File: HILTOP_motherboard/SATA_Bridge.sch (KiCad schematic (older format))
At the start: 60 parts, among them J25 DEBUG, U37 TUSB9261, U38 AT25DN512CSSHF-B, Y7 40MHz Crystal

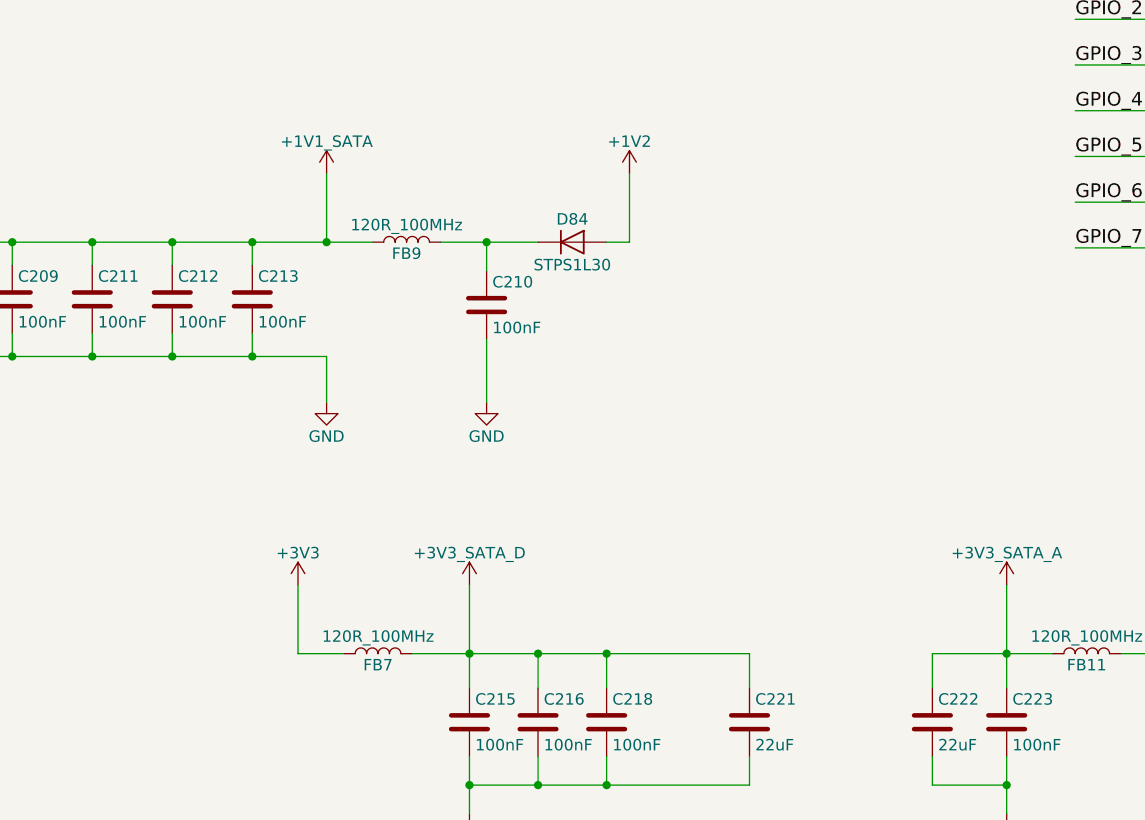
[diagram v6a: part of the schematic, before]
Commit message: DRC checks complete, all errors and warnings cleared. BOM created and parts rationalised.
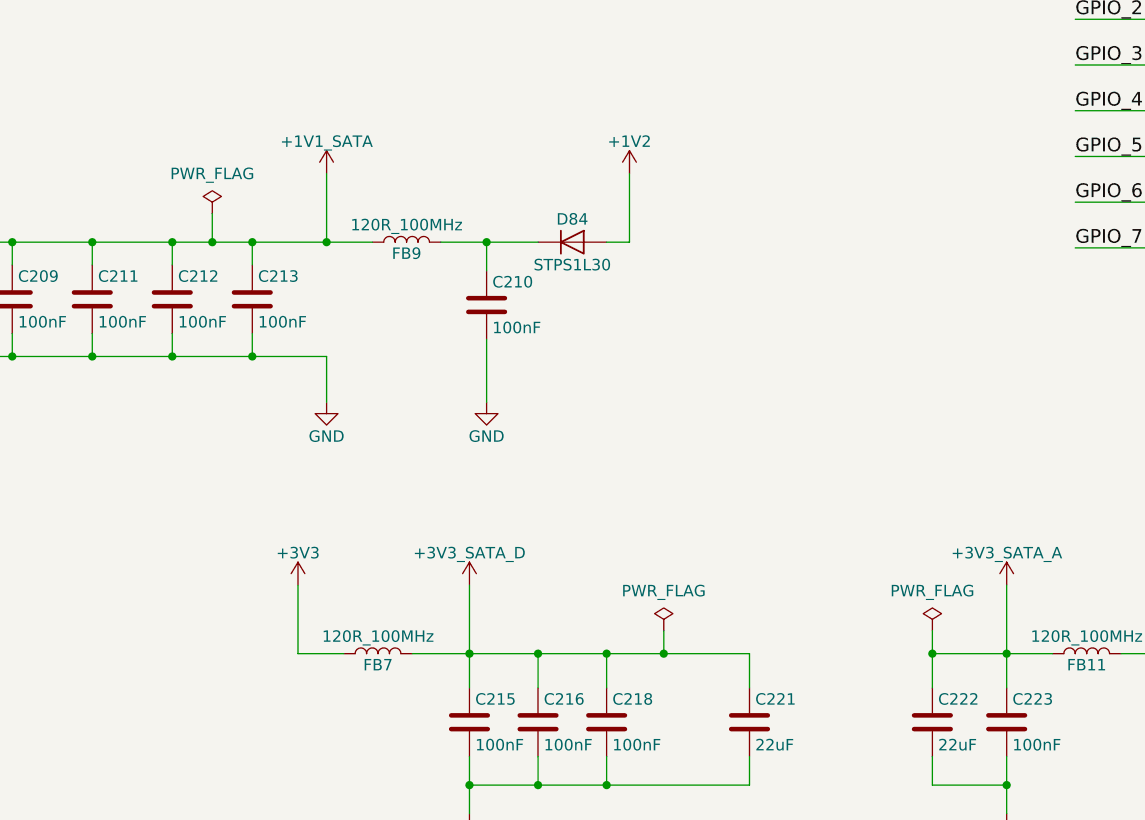
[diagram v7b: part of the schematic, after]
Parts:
- C195: Devtank 105-012 -> 105-014
- C196, C221, C222: footprint Capacitor_SMD:C_0805_2012Metric -> Capacitor_SMD:C_1206_3216Metric; Devtank 105-018 -> 105-003
- R235, R236, R237, R238, R239, R240, R241, R242: Devtank 101-024 -> 101-504
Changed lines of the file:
@@
 F 0 "C221" H 8050 10200 50  0000 L CNN
 F 1 "22uF" H 8050 10000 50  0000 L CNN
-F 2 "Capacitor_SMD:C_0805_2012Metric" H 8063 9950 50  0001 C CNN
+F 2 "Capacitor_SMD:C_1206_3216Metric" H 8063 9950 50  0001 C CNN
 F 3 "" H 8025 10100 50  0000 C CNN
-F 4 "105-018" H 8025 10100 50  0001 C CNN "Devtank"
+F 4 "105-003" H 8025 10100 50  0001 C CNN "Devtank"
 	1    8025 10100
 	1    0    0    -1
@@
 F 0 "C222" H 8850 10200 50  0000 L CNN
 F 1 "22uF" H 8850 10000 50  0000 L CNN
-F 2 "Capacitor_SMD:C_0805_2012Metric" H 8863 9950 50  0001 C CNN
+F 2 "Capacitor_SMD:C_1206_3216Metric" H 8863 9950 50  0001 C CNN
 F 3 "" H 8825 10100 50  0000 C CNN
-F 4 "105-018" H 8825 10100 50  0001 C CNN "Devtank"
+F 4 "105-003" H 8825 10100 50  0001 C CNN "Devtank"
 	1    8825 10100
 	1    0    0    -1
@@
 F 0 "C196" H 2675 8350 50  0000 L CNN
 F 1 "22uF" H 2675 8150 50  0000 L CNN
-F 2 "Capacitor_SMD:C_0805_2012Metric" H 2688 8100 50  0001 C CNN
+F 2 "Capacitor_SMD:C_1206_3216Metric" H 2688 8100 50  0001 C CNN
 F 3 "" H 2650 8250 50  0000 C CNN
-F 4 "105-018" H 2650 8250 50  0001 C CNN "Devtank"
+F 4 "105-003" H 2650 8250 50  0001 C CNN "Devtank"
 	1    2650 8250
 	1    0    0    -1
@@
 F 2 "Capacitor_SMD:C_0603_1608Metric" H 2338 8100 50  0001 C CNN
 F 3 "" H 2300 8250 50  0000 C CNN
-F 4 "105-012" H 2300 8250 50  0001 C CNN "Devtank"
+F 4 "105-014" H 2300 8250 50  0001 C CNN "Devtank"
 	1    2300 8250
 	1    0    0    -1
@@
 F 2 "Resistor_SMD:R_0402_1005Metric" V 11355 6625 50  0001 C CNN
 F 3 "" H 11425 6625 50  0000 C CNN
-F 4 "101-024" V 11425 6625 60  0001 C CNN "Devtank"
+F 4 "101-504" V 11425 6625 60  0001 C CNN "Devtank"
 	1    11425 6625
 	0    1    1    0
@@
 F 2 "Resistor_SMD:R_0402_1005Metric" V 11355 6825 50  0001 C CNN
 F 3 "" H 11425 6825 50  0000 C CNN
-F 4 "101-024" V 11425 6825 60  0001 C CNN "Devtank"
+F 4 "101-504" V 11425 6825 60  0001 C CNN "Devtank"
 	1    11425 6825
 	0    1    1    0
@@
 F 2 "Resistor_SMD:R_0402_1005Metric" V 11355 7025 50  0001 C CNN
 F 3 "" H 11425 7025 50  0000 C CNN
-F 4 "101-024" V 11425 7025 60  0001 C CNN "Devtank"
+F 4 "101-504" V 11425 7025 60  0001 C CNN "Devtank"
 	1    11425 7025
 	0    1    1    0
@@
 F 2 "Resistor_SMD:R_0402_1005Metric" V 11355 7225 50  0001 C CNN
 F 3 "" H 11425 7225 50  0000 C CNN
-F 4 "101-024" V 11425 7225 60  0001 C CNN "Devtank"
+F 4 "101-504" V 11425 7225 60  0001 C CNN "Devtank"
 	1    11425 7225
 	0    1    1    0
@@
 F 2 "Resistor_SMD:R_0402_1005Metric" V 11355 7425 50  0001 C CNN
 F 3 "" H 11425 7425 50  0000 C CNN
-F 4 "101-024" V 11425 7425 60  0001 C CNN "Devtank"
+F 4 "101-504" V 11425 7425 60  0001 C CNN "Devtank"
 	1    11425 7425
 	0    1    1    0
@@
 F 2 "Resistor_SMD:R_0402_1005Metric" V 11355 7625 50  0001 C CNN
 F 3 "" H 11425 7625 50  0000 C CNN
-F 4 "101-024" V 11425 7625 60  0001 C CNN "Devtank"
+F 4 "101-504" V 11425 7625 60  0001 C CNN "Devtank"
 	1    11425 7625
 	0    1    1    0
@@
 F 2 "Resistor_SMD:R_0402_1005Metric" V 11355 7825 50  0001 C CNN
 F 3 "" H 11425 7825 50  0000 C CNN
-F 4 "101-024" V 11425 7825 60  0001 C CNN "Devtank"
+F 4 "101-504" V 11425 7825 60  0001 C CNN "Devtank"
 	1    11425 7825
 	0    1    1    0
@@
 F 2 "Resistor_SMD:R_0402_1005Metric" V 11355 8025 50  0001 C CNN
 F 3 "" H 11425 8025 50  0000 C CNN
-F 4 "101-024" V 11425 8025 60  0001 C CNN "Devtank"
+F 4 "101-504" V 11425 8025 60  0001 C CNN "Devtank"
 	1    11425 8025
 	0    1    1    0
@@
 	5150 8000 5500 8000
 Wire Wire Line
-	5500 8000 5850 8000
+	5500 8000 5675 8000
 Wire Wire Line
 	5500 8500 5850 8500
@@
 	3000 8000 3750 8000
 Wire Wire Line
-	7400 9800 8025 9800
+	7400 9800 7650 9800
 Wire Wire Line
 	7400 10375 8025 10375
+$Comp
+L power:PWR_FLAG #FLG0131
+U 1 1 5EB53667
+P 7650 9700
+F 0 "#FLG0131" H 7650 9775 50  0001 C CNN
+F 1 "PWR_FLAG" H 7650 9874 50  0000 C CNN
+F 2 "" H 7650 9700 50  0001 C CNN
+F 3 "" H 7650 9700 50  0001 C CNN
+	1    7650 9700
+	1    0    0    -1
+$EndComp
+Wire Wire Line
+	7650 9700 7650 9800
+Connection ~ 7650 9800
+Wire Wire Line
+	7650 9800 8025 9800
+$Comp
+L power:PWR_FLAG #FLG0132
+U 1 1 5EB69213
+P 8825 9700
+F 0 "#FLG0132" H 8825 9775 50  0001 C CNN
+F 1 "PWR_FLAG" H 8825 9874 50  0000 C CNN
+F 2 "" H 8825 9700 50  0001 C CNN
+F 3 "" H 8825 9700 50  0001 C CNN
+	1    8825 9700
+	1    0    0    -1
+$EndComp
+Wire Wire Line
+	8825 9700 8825 9800
+Connection ~ 8825 9800
+$Comp
+L power:PWR_FLAG #FLG0133
+U 1 1 5EB9761C
+P 5675 7875
+F 0 "#FLG0133" H 5675 7950 50  0001 C CNN
+F 1 "PWR_FLAG" H 5675 8049 50  0000 C CNN
+F 2 "" H 5675 7875 50  0001 C CNN
+F 3 "" H 5675 7875 50  0001 C CNN
+	1    5675 7875
+	1    0    0    -1
+$EndComp
+Wire Wire Line
+	5675 7875 5675 8000
+Connection ~ 5675 8000
+Wire Wire Line
+	5675 8000 5850 8000
 $EndSCHEMATC

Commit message: tracking updates
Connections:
- net TX_N: now reaches C197.1, U37.56 (SATA_TX_N)
- net TX_P: now reaches C198.1, U37.57 (SATA_TX_P)
- net RX_N: now reaches C199.1, U37.59 (SATA_RX_N)
- net RX_P: now reaches C200.1, U37.60 (SATA_RX_P)
- net CAP_SATARXM renamed CAP_SATARX_N
- net CAP_SATARXP renamed CAP_SATARX_P
- net CAP_SATATXM renamed CAP_SATATX_P
- net CAP_SATATXP renamed CAP_SATATX_N
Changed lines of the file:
@@
 Text HLabel 9175 4750 2    60   Input ~ 0
 SATA_USB_N
+Text HLabel 2300 2400 0    60   Output ~ 0
+CAP_SATATX_N
 Text HLabel 2300 2175 0    60   Output ~ 0
-CAP_SATATXM
-Text HLabel 2300 2400 0    60   Output ~ 0
-CAP_SATATXP
+CAP_SATATX_P
 Text HLabel 2300 2625 0    60   Output ~ 0
-CAP_SATARXM
+CAP_SATARX_N
 Text HLabel 2300 2850 0    60   Output ~ 0
-CAP_SATARXP
+CAP_SATARX_P
 $Comp
 L device:C C197
@@
 Wire Wire Line
 	5675 8000 5850 8000
+Text Label 3600 2450 0    60   ~ 0
+TX_N
+Text Label 3600 2550 0    60   ~ 0
+TX_P
+Text Label 3600 2750 0    60   ~ 0
+RX_N
+Text Label 3600 2850 0    60   ~ 0
+RX_P
 $EndSCHEMATC
